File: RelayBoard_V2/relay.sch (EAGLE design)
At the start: 30 parts, among them K1 T9AS1D12-5, K2 T9AS1D12-5, T1 2N2222, T2 2N2222, T3 2N2222, T4 2N2222, X1 22-23-2021

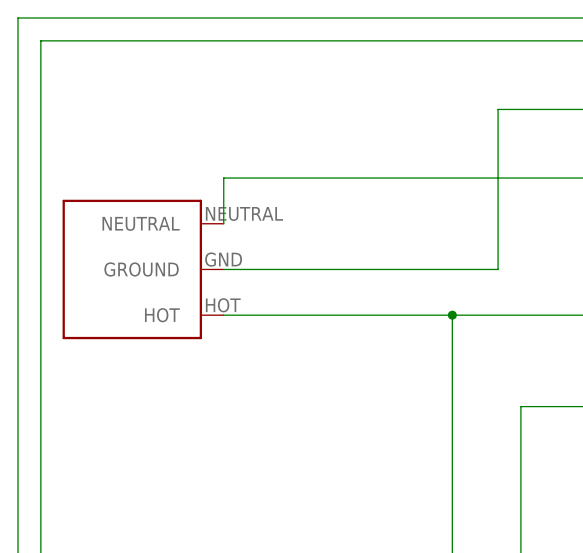
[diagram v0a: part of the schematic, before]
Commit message: flipped relays and repositioned power receptacles
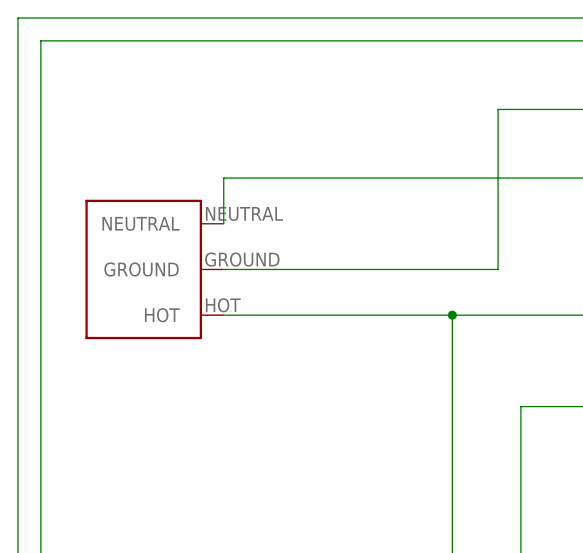
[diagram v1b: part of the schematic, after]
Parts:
- removed U$5: IEC_MALE, BloomWall:IEC_MALE
- added U$12: MAIN, BloomWall:MAIN
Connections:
- net N$19: now also U$12.HOT; no longer U$5.HOT
- net N$20: now also U$12.NEUTRAL; no longer U$5.NEUTRAL
- net PGND: now also U$12.GROUND; no longer U$5.GROUND
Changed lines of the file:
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@@
 <part name="U$6" library="BloomWall" deviceset="IEC_FEMALE" device=""/>
 <part name="U$7" library="BloomWall" deviceset="IEC_FEMALE" device=""/>
-<part name="U$5" library="BloomWall" deviceset="IEC_MALE" device=""/>
+<part name="U$12" library="BloomWall" deviceset="MAIN" device=""/>
 </parts>
 <sheets>
@@
 <instance part="U$6" gate="G$1" x="50.8" y="96.52" rot="R270"/>
 <instance part="U$7" gate="G$1" x="50.8" y="20.32" rot="R270"/>
-<instance part="U$5" gate="G$1" x="-116.84" y="109.22"/>
+<instance part="U$12" gate="G$1" x="-114.3" y="109.22"/>
 </instances>
 <busses>
@@
 <wire x1="124.46" y1="48.26" x2="43.18" y2="48.26" width="0.1524" layer="91"/>
 <wire x1="43.18" y1="48.26" x2="43.18" y2="53.34" width="0.1524" layer="91"/>
-<pinref part="U$5" gate="G$1" pin="HOT"/>
+<pinref part="U$12" gate="G$1" pin="HOT"/>
 </segment>
 </net>
@@
 <pinref part="U$6" gate="G$1" pin="NEUTRAL"/>
 <pinref part="U$7" gate="G$1" pin="NEUTRAL"/>
-<pinref part="U$5" gate="G$1" pin="NEUTRAL"/>
+<pinref part="U$12" gate="G$1" pin="NEUTRAL"/>
 </segment>
 </net>
@@
 <pinref part="U$6" gate="G$1" pin="GND"/>
 <pinref part="U$7" gate="G$1" pin="GND"/>
-<pinref part="U$5" gate="G$1" pin="GROUND"/>
-</segment>
-</net>
+<pinref part="U$12" gate="G$1" pin="GROUND"/>
+</segment>
+</net>

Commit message: GND pour and add gerbers
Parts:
- renumbered U$8 to MUX
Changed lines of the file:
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@@
 <part name="U$17" library="BloomWall" deviceset="RAC02-05SC_ACDCCONVERTER" device=""/>
 <part name="X1" library="con-molex" deviceset="22-23-2021" device=""/>
-<part name="U$8" library="BloomWall" deviceset="7HC4052_MUX" device=""/>
+<part name="MUX" library="BloomWall" deviceset="7HC4052_MUX" device=""/>
 <part name="U$9" library="BloomWall" deviceset="ATLAS_DO_WITH_ICON" device=""/>
 <part name="U$10" library="BloomWall" deviceset="ATLAS_PH_WITH_ICON" device=""/>
@@
 <instance part="X1" gate="-1" x="7.62" y="101.6"/>
 <instance part="X1" gate="-2" x="7.62" y="99.06"/>
-<instance part="U$8" gate="G$1" x="274.32" y="66.04"/>
+<instance part="MUX" gate="G$1" x="274.32" y="66.04"/>
 <instance part="U$9" gate="G$1" x="327.66" y="93.98" rot="R90"/>
 <instance part="U$10" gate="G$1" x="327.66" y="76.2" rot="R90"/>
@@
 <net name="N$7" class="0">
 <segment>
-<pinref part="U$8" gate="G$1" pin="X-COM"/>
+<pinref part="MUX" gate="G$1" pin="X-COM"/>
 <wire x1="261.62" y1="78.74" x2="205.74" y2="78.74" width="0.1524" layer="91"/>
 <pinref part="U$1" gate="G$1" pin="GPIO13"/>
@@
 <wire x1="205.74" y1="81.28" x2="254" y2="81.28" width="0.1524" layer="91"/>
 <wire x1="254" y1="81.28" x2="254" y2="73.66" width="0.1524" layer="91"/>
-<pinref part="U$8" gate="G$1" pin="Y-COM"/>
+<pinref part="MUX" gate="G$1" pin="Y-COM"/>
 <wire x1="254" y1="73.66" x2="261.62" y2="73.66" width="0.1524" layer="91"/>
 <pinref part="U$1" gate="G$1" pin="GPIO6"/>
@@
 <net name="N$22" class="0">
 <segment>
-<pinref part="U$8" gate="G$1" pin="2Y"/>
+<pinref part="MUX" gate="G$1" pin="2Y"/>
 <pinref part="U$11" gate="G$1" pin="TX"/>
 <wire x1="284.48" y1="58.42" x2="317.5" y2="58.42" width="0.1524" layer="91"/>
@@
 <net name="N$23" class="0">
 <segment>
-<pinref part="U$8" gate="G$1" pin="2X"/>
+<pinref part="MUX" gate="G$1" pin="2X"/>
 <pinref part="U$11" gate="G$1" pin="RX"/>
 <wire x1="284.48" y1="63.5" x2="317.5" y2="63.5" width="0.1524" layer="91"/>
@@
 <net name="N$24" class="0">
 <segment>
-<pinref part="U$8" gate="G$1" pin="1Y"/>
+<pinref part="MUX" gate="G$1" pin="1Y"/>
 <wire x1="284.48" y1="68.58" x2="304.8" y2="68.58" width="0.1524" layer="91"/>
 <wire x1="304.8" y1="68.58" x2="304.8" y2="76.2" width="0.1524" layer="91"/>
@@
 <net name="N$25" class="0">
 <segment>
-<pinref part="U$8" gate="G$1" pin="1X"/>
+<pinref part="MUX" gate="G$1" pin="1X"/>
 <wire x1="284.48" y1="73.66" x2="302.26" y2="73.66" width="0.1524" layer="91"/>
 <wire x1="302.26" y1="73.66" x2="302.26" y2="81.28" width="0.1524" layer="91"/>
@@
 <net name="N$26" class="0">
 <segment>
-<pinref part="U$8" gate="G$1" pin="0Y"/>
+<pinref part="MUX" gate="G$1" pin="0Y"/>
 <wire x1="284.48" y1="78.74" x2="299.72" y2="78.74" width="0.1524" layer="91"/>
 <wire x1="299.72" y1="78.74" x2="299.72" y2="93.98" width="0.1524" layer="91"/>
@@
 <net name="N$27" class="0">
 <segment>
-<pinref part="U$8" gate="G$1" pin="0X"/>
+<pinref part="MUX" gate="G$1" pin="0X"/>
 <wire x1="284.48" y1="83.82" x2="297.18" y2="83.82" width="0.1524" layer="91"/>
 <wire x1="297.18" y1="83.82" x2="297.18" y2="99.06" width="0.1524" layer="91"/>
@@
 <wire x1="233.68" y1="88.9" x2="243.84" y2="88.9" width="0.1524" layer="91"/>
 <wire x1="243.84" y1="88.9" x2="243.84" y2="63.5" width="0.1524" layer="91"/>
-<pinref part="U$8" gate="G$1" pin="B"/>
+<pinref part="MUX" gate="G$1" pin="B"/>
 <wire x1="243.84" y1="63.5" x2="261.62" y2="63.5" width="0.1524" layer="91"/>
 <pinref part="R8" gate="G$1" pin="1"/>
@@
 <net name="N$29" class="0">
 <segment>
-<pinref part="U$8" gate="G$1" pin="A"/>
+<pinref part="MUX" gate="G$1" pin="A"/>
 <wire x1="261.62" y1="68.58" x2="248.92" y2="68.58" width="0.1524" layer="91"/>
 <wire x1="248.92" y1="68.58" x2="248.92" y2="91.44" width="0.1524" layer="91"/>
@@
 <wire x1="238.76" y1="48.26" x2="238.76" y2="38.1" width="0.1524" layer="91"/>
 <wire x1="238.76" y1="38.1" x2="309.88" y2="38.1" width="0.1524" layer="91"/>
-<pinref part="U$8" gate="G$1" pin="GND"/>
+<pinref part="MUX" gate="G$1" pin="GND"/>
 <wire x1="261.62" y1="48.26" x2="238.76" y2="48.26" width="0.1524" layer="91"/>
 <junction x="238.76" y="48.26"/>
-<pinref part="U$8" gate="G$1" pin="VEE"/>
+<pinref part="MUX" gate="G$1" pin="VEE"/>
 <wire x1="261.62" y1="53.34" x2="238.76" y2="53.34" width="0.1524" layer="91"/>
 <junction x="238.76" y="53.34"/>
-<pinref part="U$8" gate="G$1" pin="INH"/>
+<pinref part="MUX" gate="G$1" pin="INH"/>
 <wire x1="261.62" y1="58.42" x2="238.76" y2="58.42" width="0.1524" layer="91"/>
 <junction x="238.76" y="58.42"/>
@@
 <wire x1="337.82" y1="71.12" x2="350.52" y2="71.12" width="0.1524" layer="91"/>
 <junction x="350.52" y="71.12"/>
-<pinref part="U$8" gate="G$1" pin="VCC"/>
+<pinref part="MUX" gate="G$1" pin="VCC"/>
 <wire x1="261.62" y1="83.82" x2="256.54" y2="83.82" width="0.1524" layer="91"/>
 <wire x1="256.54" y1="83.82" x2="256.54" y2="111.76" width="0.1524" layer="91"/>

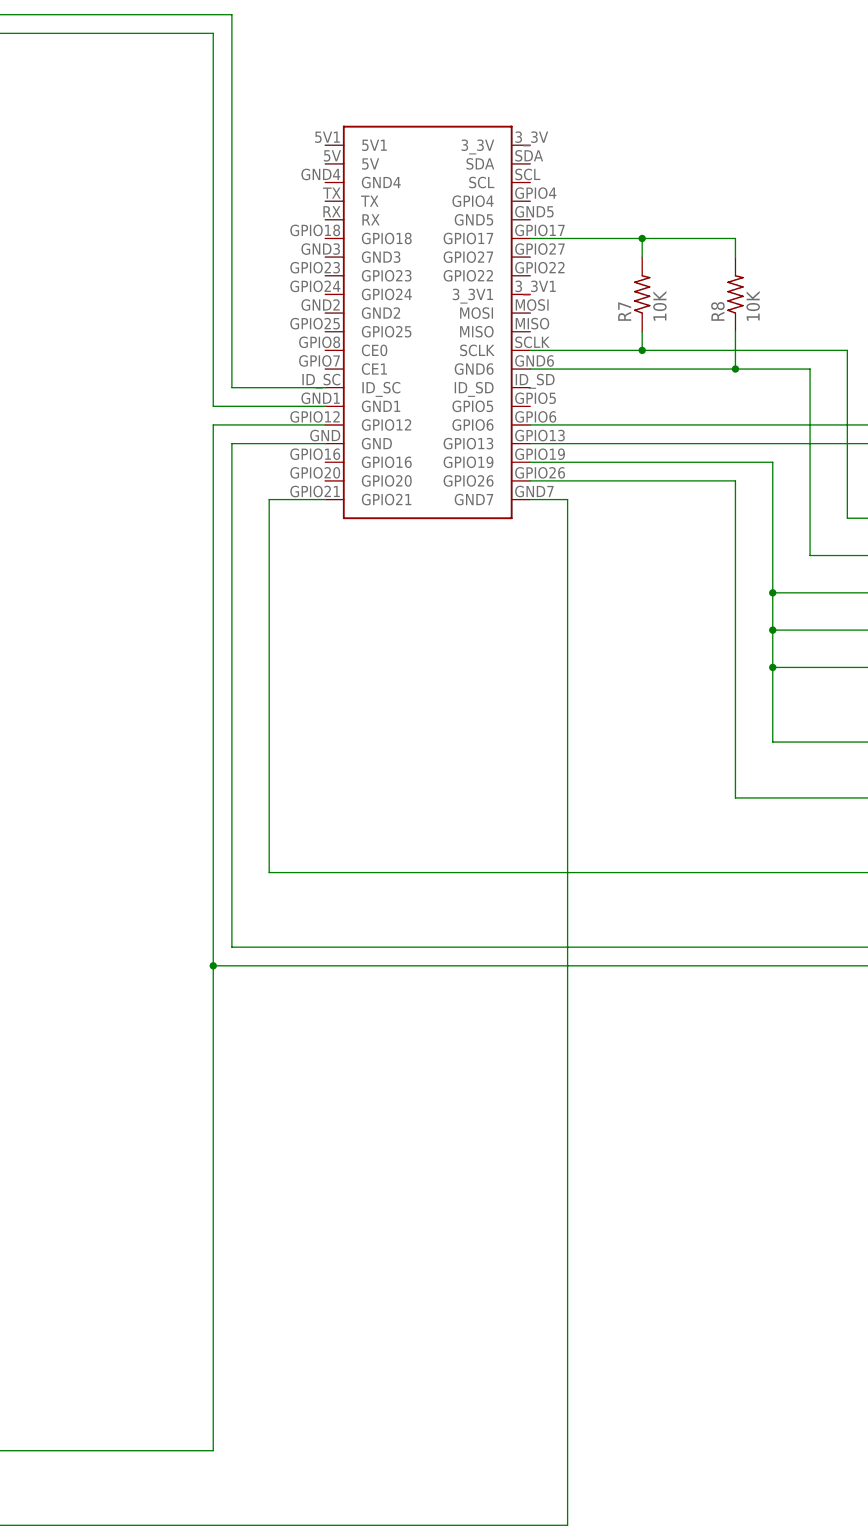
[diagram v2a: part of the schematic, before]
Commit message: Reduced DPI of silkscreen to OSH Park can actually fabricate them. New gerbers.
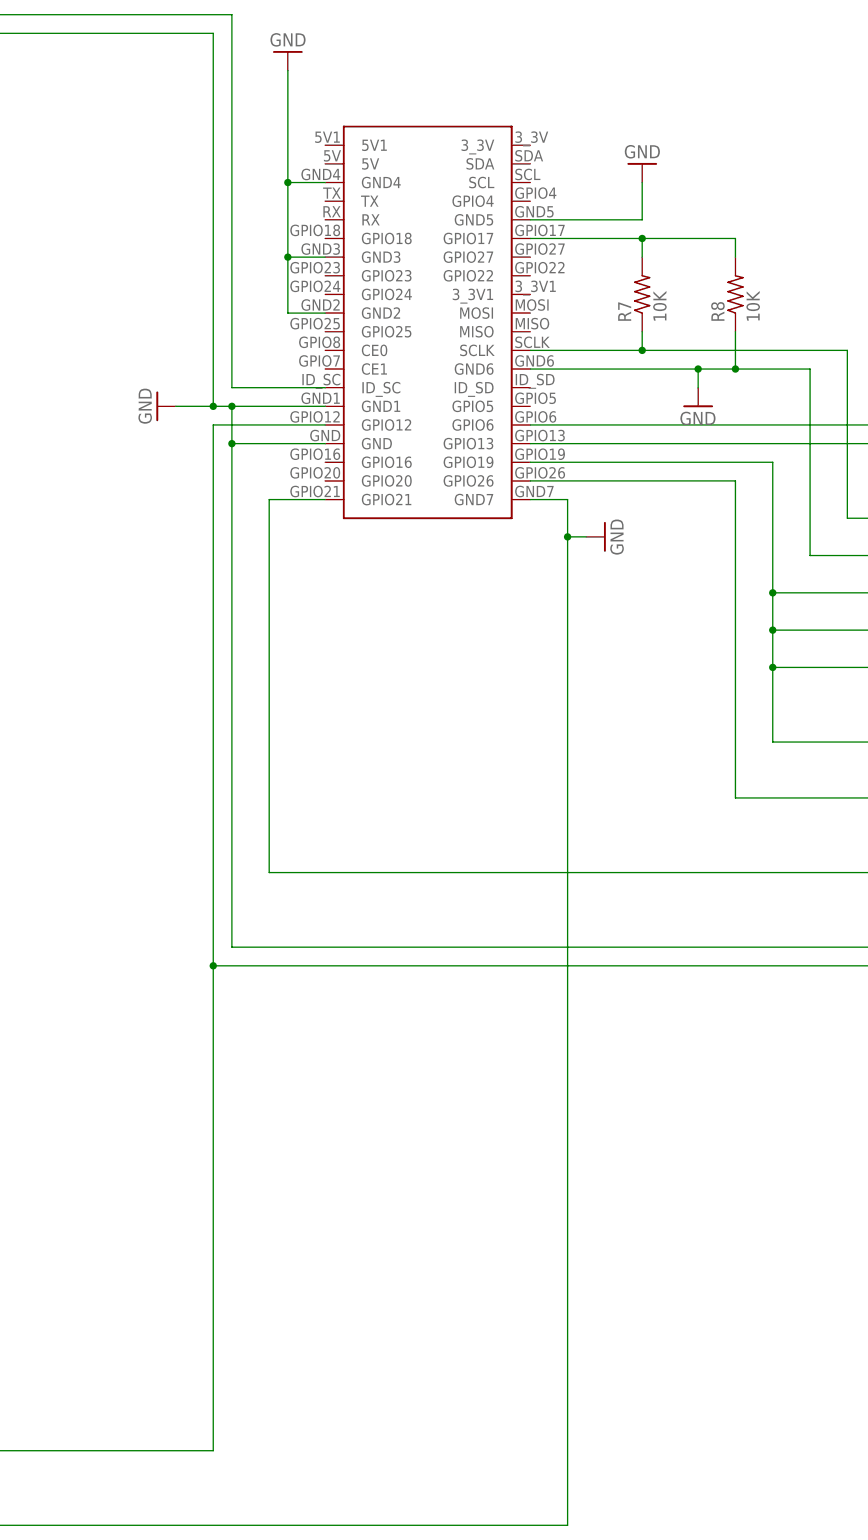
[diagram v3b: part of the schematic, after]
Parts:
- removed U$11: ATLAS_PPM_WITH_ICON, BloomWall:ATLAS_PPM_WITH_ICON
- added U$5: ATLAS_DO_WITH_ICON, BloomWall:ATLAS_DO_WITH_ICON
- U$9: value ATLAS_DO_WITH_ICON -> ATLAS_PPM_WITH_ICON; device BloomWall:ATLAS_DO_WITH_ICON -> BloomWall:ATLAS_PPM_WITH_ICON
- renumbered U$10 to U$8
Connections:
- removed net N$2: R1.2, U$1.GND1
- removed net N$28: MUX.B, R8.1, U$1.GND6
- removed net N$35: R9.1, U$1.GND, U$4.P5
- removed net N$6: R3.2, R4.2, U$1.GND7
- new net GND: MUX.B, R1.2, R3.2, R4.2, R8.1, R9.1, U$1.GND, U$1.GND1, U$1.GND2, U$1.GND3, U$1.GND4, U$1.GND5, U$1.GND6, U$1.GND7, U$4.P5
- net N$22: now also U$9.TX; no longer U$11.TX
- net N$23: now also U$9.RX; no longer U$11.RX
- net N$26: now also U$5.TX; no longer U$9.TX
- net N$27: now also U$5.RX; no longer U$9.RX
- net N$30: now also U$5.GND; no longer U$11.GND
- net N$31: now also U$5.PGND; no longer U$9.PGND
- net N$33: now also U$5.VCC; no longer U$11.VCC
- net N$37: now also U$9.PRB; no longer U$11.PRB
- net N$38: now also U$9.PRB2; no longer U$11.PRB2
- net N$41: now also U$5.PRB; no longer U$9.PRB
